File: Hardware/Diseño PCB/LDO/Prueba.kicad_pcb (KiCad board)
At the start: 2 copper layers, 98.5 x 100.5 mm, 57 parts, among them Q1 2N3904, Q10 BC557, Q11 BC547, Q12 BC557, Q13 BC557, Q14 BC547, Q15 BC557, Q16 BC547, Q17 BC557, Q18 BC547, Q19 BC547, Q2 BC547, Q3 BC547, Q4 BC557, Q5 BC557, Q6 BC547, Q7 BC547, Q8 IRF4905, Q9 BC547, U1 TL431LP, U4 LM324

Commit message: Diseño PCB
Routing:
- net GND: track 331.5 -> 335.8 mm
- added copper zone on B.Cu, net GND
- added copper zone on F.Cu, net GND
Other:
- board text added: "Compensación"
- board text removed: "Compensacion"
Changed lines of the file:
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@@
 	)
 	(paper "A4")
+	(title_block
+		(title "Diseño de PCB : LDO Grupo 7")
+	)
 	(layers
 		(0 "F.Cu" signal)
@@
 		)
 	)
-	(gr_text "Compensacion\n\n"
+	(gr_text "Compensación\n\n"
 		(at 154.5 95 0)
 		(layer "F.SilkS")
@@
 	)
 	(segment
-		(start 166.36 78.0002)
-		(end 166.36 78.0017)
+		(start 116.19 122.4017)
+		(end 116.19 121)
 		(width 1)
 		(layer "B.Cu")
@@
 	)
 	(segment
-		(start 116.4817 77.6)
-		(end 118.26 77.6)
+		(start 166.36 78.0002)
+		(end 166.36 78.0017)
 		(width 1)
 		(layer "B.Cu")
@@
 	)
 	(segment
-		(start 116.19 122.4017)
-		(end 116.19 121)
+		(start 116.4817 77.6)
+		(end 118.26 77.6)
 		(width 1)
 		(layer "B.Cu")
@@
 	)
 	(segment
-		(start 116.19 122.4017)
-		(end 107.4017 122.4017)
+		(start 133.81 121)
+		(end 137.1875 124.3775)
 		(width 1)
 		(layer "B.Cu")
@@
 	)
 	(segment
-		(start 133.81 121)
-		(end 137.1875 124.3775)
+		(start 118.5 124)
+		(end 109 124)
 		(width 1)
 		(layer "B.Cu")
@@
 	)
 	(segment
-		(start 109.6482 137.8083)
-		(end 115.435 137.8083)
+		(start 133.81 121)
+		(end 130.81 124)
 		(width 1)
 		(layer "B.Cu")
@@
 	)
 	(segment
-		(start 107.4017 122.4017)
-		(end 106 121)
+		(start 109.6482 137.8083)
+		(end 115.435 137.8083)
 		(width 1)
 		(layer "B.Cu")
@@
 	)
 	(segment
-		(start 132.4083 122.4017)
+		(start 117.7883 124)
 		(end 116.19 122.4017)
 		(width 1)
@@
 	)
 	(segment
+		(start 130.81 124)
+		(end 117.7883 124)
+		(width 1)
+		(layer "B.Cu")
+		(net "GND")
+	)
+	(segment
+		(start 109 124)
+		(end 106 121)
+		(width 1)
+		(layer "B.Cu")
+		(net "GND")
+	)
+	(segment
 		(start 159.5784 78.0017)
 		(end 166.3585 78.0017)
@@
 	)
 	(segment
-		(start 133.81 121)
-		(end 132.4083 122.4017)
-		(width 1)
-		(layer "B.Cu")
-		(net "GND")
-	)
-	(segment
 		(start 179.3924 78.6166)
 		(end 182.2758 81.5)
@@
 		(net "Net-(Q2-C)")
 	)
+	(zone
+		(net "GND")
+		(layers "F.Cu" "B.Cu")
+		(hatch edge 0.5)
+		(connect_pads
+			(clearance 0.5)
+		)
+		(min_thickness 0.25)
+		(fill
+			(mode hatch)
+			(thermal_gap 0.5)
+			(thermal_bridge_width 0.5)
+			(island_removal_mode 0)
+			(hatch_thickness 1)
+			(hatch_gap 1.5)
+			(hatch_orientation 0)
+			(hatch_border_algorithm hatch_thickness)
+			(hatch_min_hole_area 0.15)
+		)
+		(polygon
+			(pts
+				(xy 104 59.5) (xy 192 60) (xy 192 141) (xy 102.5 142) (xy 103.5 59.5)
+			)
+		)
+	)
 	(embedded_fonts no)

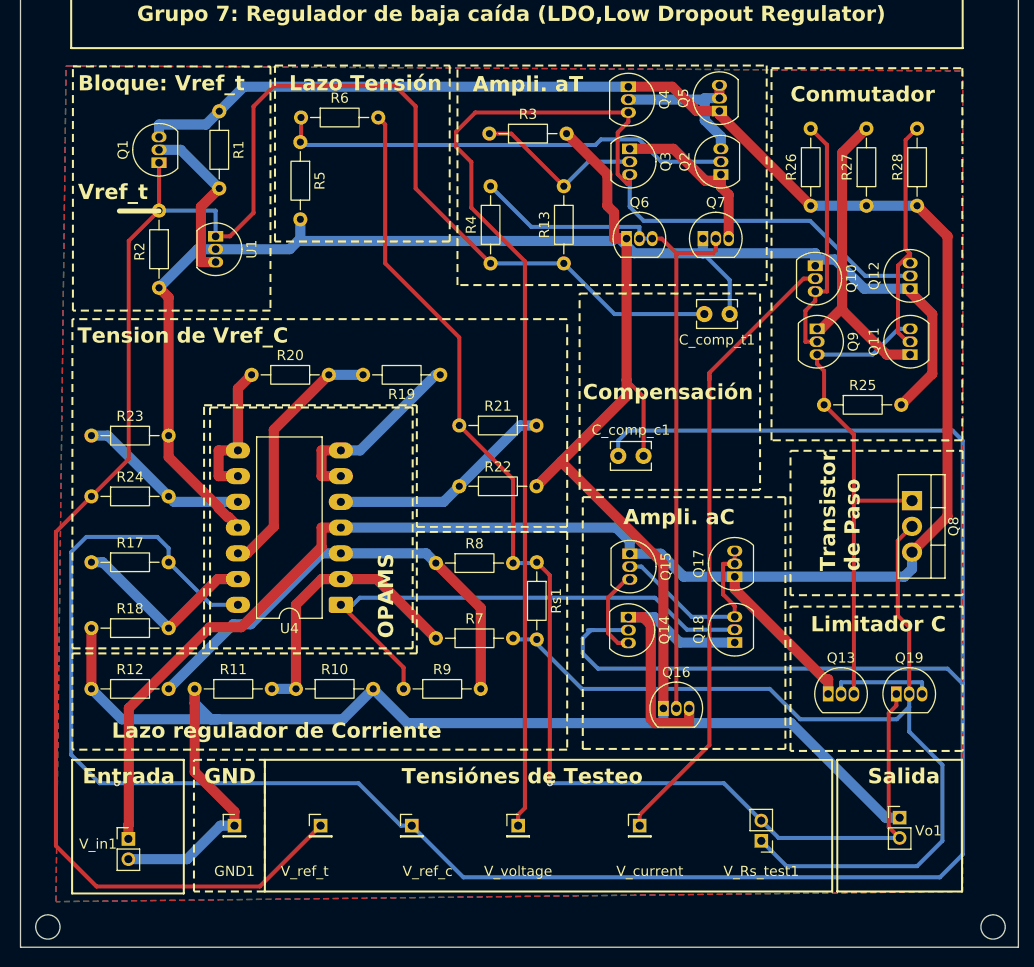
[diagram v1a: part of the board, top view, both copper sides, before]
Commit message: Diseño PCB: Modificacion grosor de pistas 0.8 mm
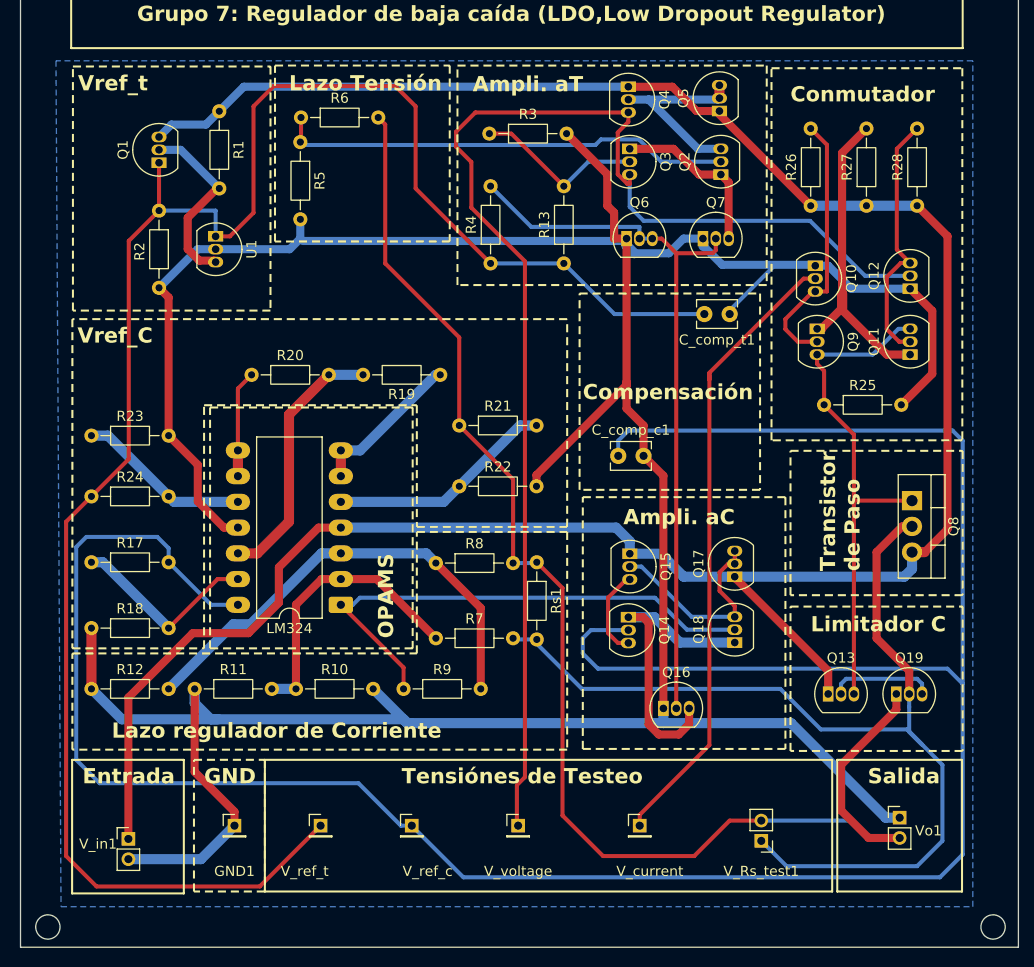
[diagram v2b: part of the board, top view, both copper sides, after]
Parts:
- renumbered U4 to LM324
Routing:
- net -V_Rs: track 126.0 -> 136.2 mm, vias 1 -> 0
- net +V_Rs: track 96.6 -> 102.5 mm
- net Net-(U4B--): track 19.2 -> 15.4 mm
- net Net-(U4C--): track 14.4 -> 10.6 mm
- net Net-(Q2-C): track 15.9 -> 19.5 mm
- net Net-(Q10-E): track 24.4 -> 26.6 mm
- net Net-(Q11-B): track 23.8 -> 25.5 mm
- net Net-(Q14-E): track 28.8 -> 30.2 mm
- net GND: track 335.8 -> 334.6 mm
- net Net-(Q1-B): track 17.0 -> 18.2 mm
- net Vcc: track 238.6 -> 239.6 mm
- net Vref_c: track 257.4 -> 256.4 mm, vias 1 -> 0
- net Vref: track 184.6 -> 183.8 mm
- net Net-(U4D-+): track 25.3 -> 25.8 mm
- removed copper zone on F.Cu, net GND
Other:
- board text added: "Vref_C"
- board text removed: "Bloque: Vref_t"
- board text removed: "Tension de Vref_C"

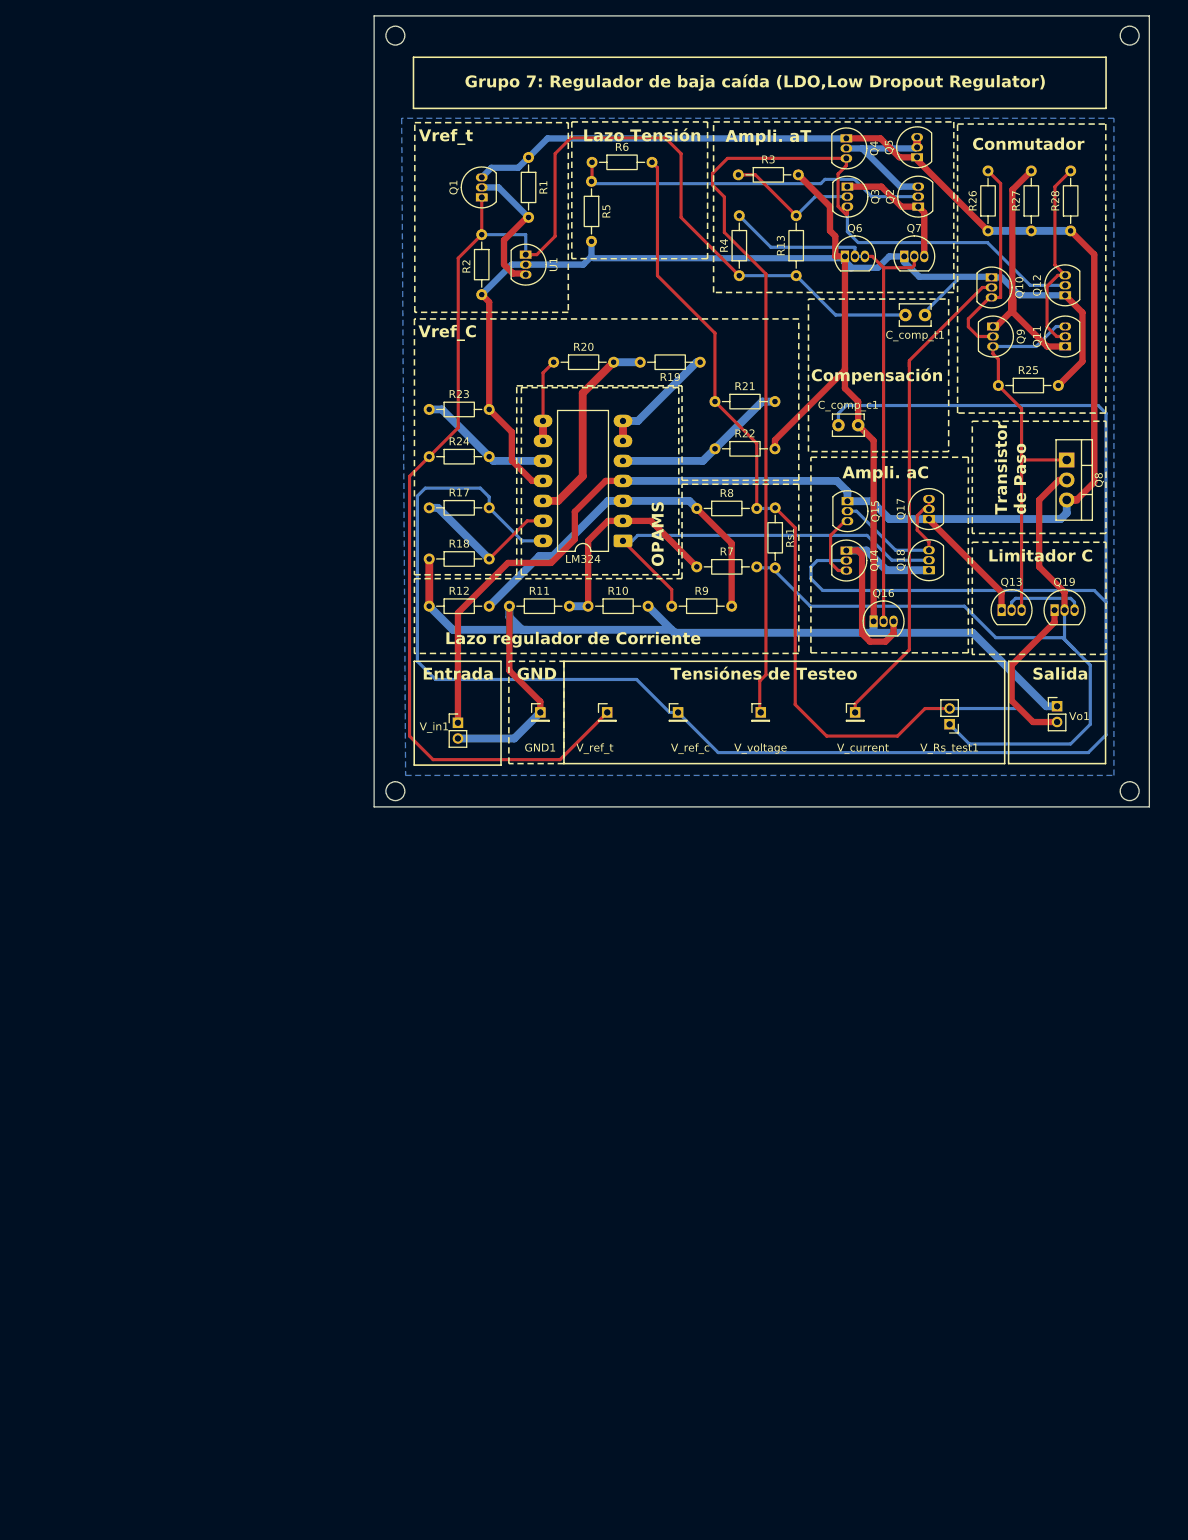
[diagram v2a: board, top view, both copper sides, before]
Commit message: Diseño PCB: Correcciones profe y añadi preset
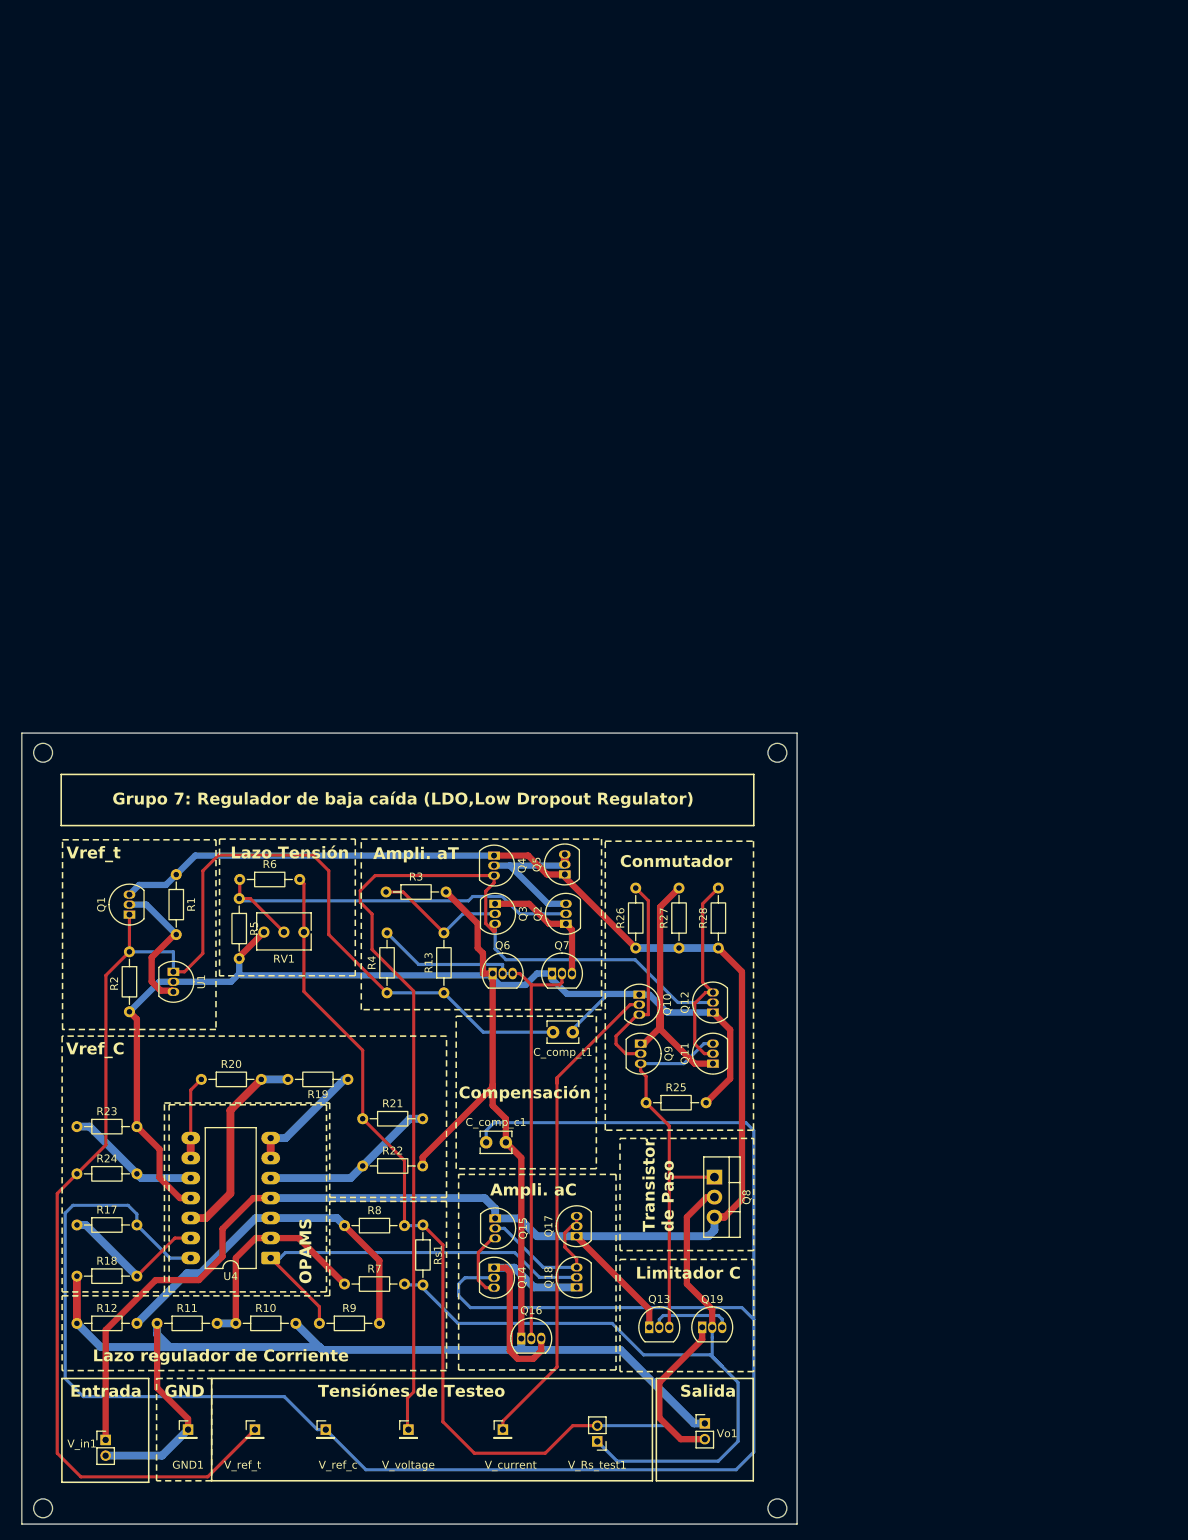
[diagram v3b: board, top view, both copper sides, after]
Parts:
- added RV1: Preset, Potentiometer_THT:Potentiometer_Bourns_3266Y_Vertical, F.Cu at (85.0, 162.4)
- moved Q14 101.5 mm to (114.2, 205.0)
- moved Q16 101.5 mm to (117.7, 214.0)
- moved Q17 101.5 mm to (124.7, 201.0)
- moved Q18 101.5 mm to (124.7, 207.5)
- moved Q6 101.5 mm to (114.1, 167.7)
- moved Q7 101.5 mm to (121.6, 167.7)
- moved C_comp_c1 101.5 mm to (113.2, 189.1)
- moved C_comp_t1 101.5 mm to (124.2, 175.1)
- moved GND1 101.5 mm to (75.4, 225.6)
- moved Q1 101.5 mm to (67.9, 160.2)
- moved Q11 101.5 mm to (142.0, 179.1)
- moved Q12 101.5 mm to (142.0, 172.6)
- moved Q13 101.5 mm to (134.0, 212.6)
- moved Q15 101.5 mm to (114.4, 198.8)
- moved Q19 101.5 mm to (140.7, 212.6)
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- renumbered LM324 to U4
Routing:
- net VF_fv: track 45.2 -> 52.7 mm
- net GND: track 334.6 -> 339.2 mm
- removed copper zone on B.Cu, net GND
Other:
- board text added: "Red señal: 0.4 mm Red Alimentación y potencia : 0.8 mm"
- board text added: "Ref. tensión: TL431, Q1, R1-R2 Ref. corriente: U4B-U4D (LM324), R17-R24 Lazo corriente: U4A (LM324), Rs1, R7-R12 Lazo tensión: R5-R6 Amp. tensión (A\textsubscript{T}): Q2-Q7, R3, R4, R13 Amp. corriente (A\textsubscript{C}): Q14-Q18 Conmutador: Q9-Q12, R25-R28 Limitador: Q13, Q19 Transistor de paso: Q8"
- board text removed: "Tension de referencia para lazo de tension Q1 R1,R2 TL431 Tension de referencia lazo de corriente LM324 U4B, U4C, U4D R17,R18,R19,R20,R21,R22,R23,R24 Lazo regulador de corriente: LM324 UA R12, R9 , R8 , R7 , Rs1 , R11, R10 Lazo reg de tension R6, R5 Amplificador aT Q3,Q2,Q4,Q5,Q6,Q7 R13,R3,R4 Amplificador aC Q14,Q18,Q15,Q17,Q16 Conmutador analogico R25,R26,R27,R28 Q9,Q11,Q10,Q12 limitador de corr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"

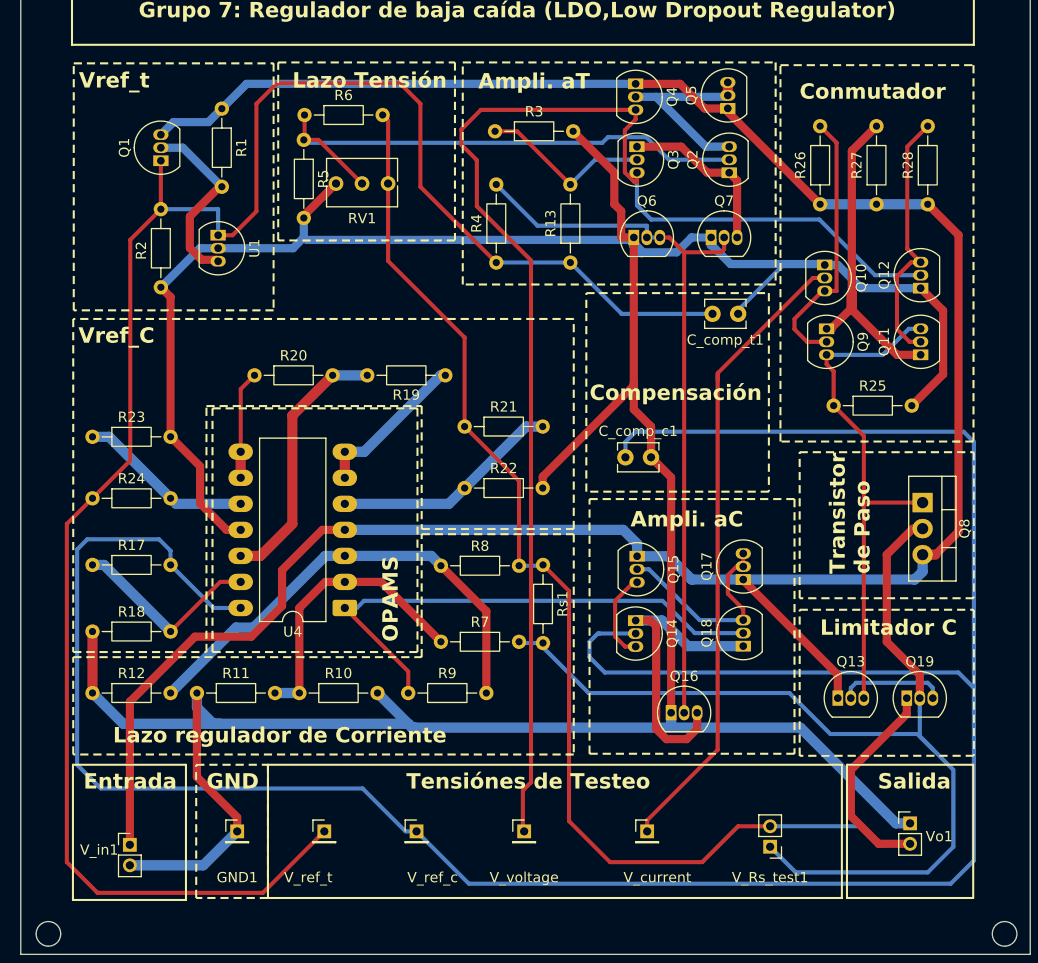
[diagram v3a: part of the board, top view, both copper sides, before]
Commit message: Diseño PCB: Disipador, modelo 3D
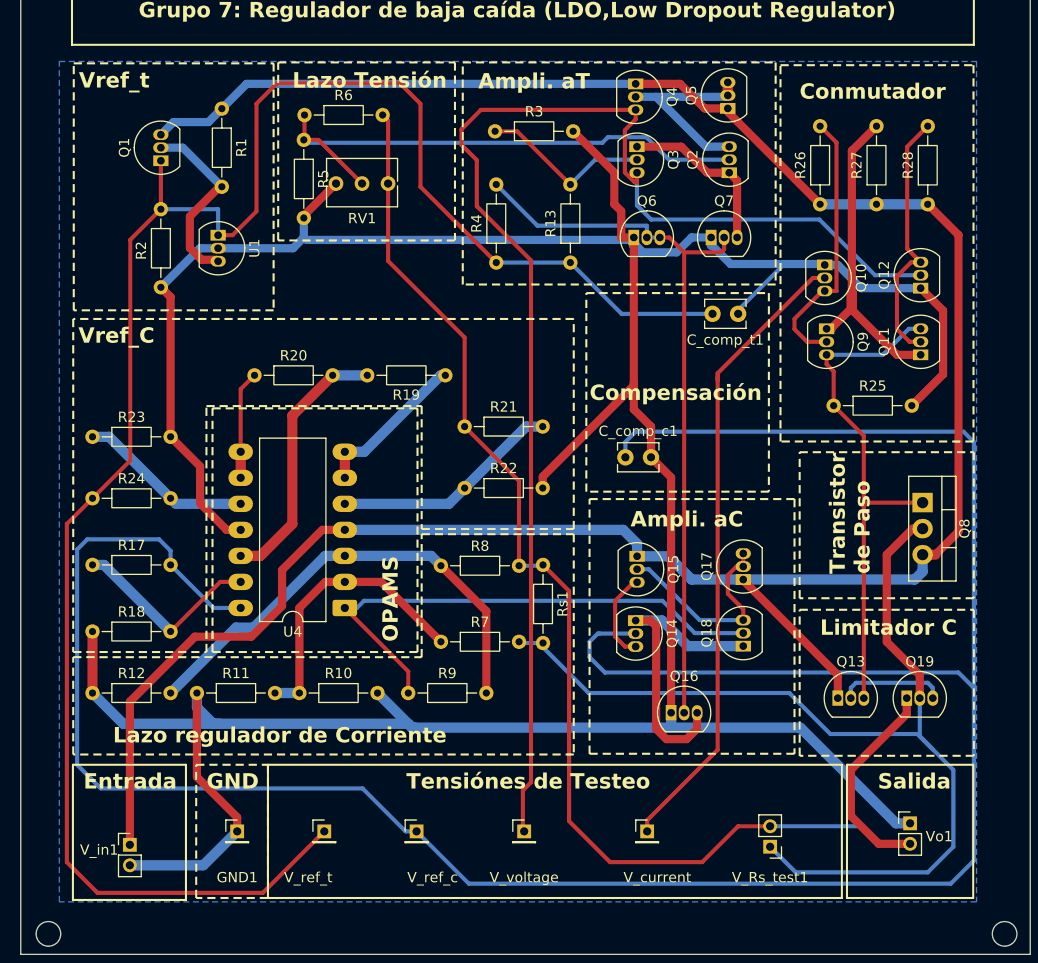
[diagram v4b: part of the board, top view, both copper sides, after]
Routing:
- added copper zone on B.Cu, net GND
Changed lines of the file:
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@@
 			)
 		)
+		(model "${KICAD10_3DMODEL_DIR}/Heatsink.3dshapes/Heatsink_Stonecold_HS-132_32x14mm_2xFixation1.5mm.step"
+			(offset
+				(xyz 2.5 1.5 0)
+			)
+			(scale
+				(xyz 0.7 0.6 0.85)
+			)
+			(rotate
+				(xyz -0 -0 -0)
+			)
+		)
 	)
 	(footprint "Package_TO_SOT_THT:TO-92_Inline"
@@
 		(net "Net-(Q2-C)")
 	)
+	(zone
+		(net "GND")
+		(layer "B.Cu")
+		(hatch full 0.5)
+		(connect_pads
+			(clearance 0.5)
+		)
+		(min_thickness 0.25)
+		(fill yes
+			(thermal_gap 0.5)
+			(thermal_bridge_width 0.5)
+			(island_removal_mode 1)
+		)
+		(polygon
+			(pts
+				(xy 147.5 150.5) (xy 147.5 232.5) (xy 58 232.5) (xy 58 150.5)
+			)
+		)
+	)
 	(embedded_fonts no)
